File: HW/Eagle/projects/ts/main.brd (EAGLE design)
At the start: 80 x 45 mm, 46 parts, among them IC1 4050D, Q1 20 MHz, T1 IRFZ24N, T2 IRFZ24N, U1 ATMEGA328P-PU, U2 LM2576T, U3 HT7533, U4 LM75

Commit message: [HW] Minor change
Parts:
- removed R5: 0R, rcl:R0805
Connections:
- removed net N$1: C9.+, R5.2, U3.3
- net +3V3: now also C9.+, U3.3; no longer R5.1
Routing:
- net +3V3: track 29.6 -> 38.8 mm
- net N$1: track 7.34 -> 0.00 mm
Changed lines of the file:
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@@
 <attribute name="OC_NEWARK" value="unknown" x="34.5" y="39.5" size="1.778" layer="27" display="off"/>
-</element>
-<element name="R5" library="rcl" package="R0805" value="0R" x="11" y="40.5" smashed="yes" rot="R180">
-<attribute name="NAME" x="9.365" y="41.77" size="1.27" layer="25"/>
-<attribute name="VALUE" x="11.635" y="43.04" size="1.27" layer="27" rot="R180"/>
 </element>
 <element name="C11" library="rcl" package="C0805" value="100nF" x="29" y="30" smashed="yes" rot="R90">
@@
 <contactref element="RESET" pad="3"/>
 <via x="9.5" y="38.75" extent="1-16" drill="0.5"/>
-<via x="6" y="41" extent="1-16" drill="0.5"/>
+<via x="5" y="41" extent="1-16" drill="0.5"/>
 <via x="5" y="31" extent="1-16" drill="0.5"/>
-<via x="12.5" y="38.75" extent="1-16" drill="0.5"/>
+<via x="9.25" y="44" extent="1-16" drill="0.5"/>
 <contactref element="IC1" pad="7"/>
 <contactref element="UART" pad="1"/>
@@
 <via x="45" y="6" extent="1-16" drill="0.5"/>
 <via x="40.5" y="1.5" extent="1-16" drill="0.5"/>
-<via x="7.5" y="35.5" extent="1-16" drill="0.5"/>
+<via x="7.5" y="36" extent="1-16" drill="0.5"/>
 <via x="57.25" y="32.25" extent="1-16" drill="0.5"/>
 <via x="41.25" y="9.75" extent="1-16" drill="0.5"/>
@@
 <wire x1="28" y1="26" x2="24" y2="22" width="1.3" layer="16"/>
 <wire x1="24" y1="22" x2="19.5" y2="22" width="1.3" layer="16"/>
-<wire x1="11.46" y1="26.5" x2="11.46" y2="31.04" width="0.4" layer="16"/>
-<wire x1="11.46" y1="31.04" x2="11" y2="31.5" width="0.4" layer="16"/>
-<wire x1="11" y1="31.5" x2="11" y2="34.595" width="0.4" layer="16"/>
 <wire x1="17.55" y1="43" x2="12.5" y2="43" width="0.25" layer="1"/>
 <wire x1="12.5" y1="43" x2="12" y2="42.5" width="0.25" layer="1"/>
@@
 <wire x1="62.375" y1="18.125" x2="63.425" y2="18.125" width="1" layer="16"/>
 <wire x1="63.425" y1="18.125" x2="63.5" y2="18.2" width="1" layer="16"/>
+<wire x1="11.46" y1="26.5" x2="11.46" y2="31.04" width="0.5" layer="16"/>
+<wire x1="11.46" y1="31.04" x2="11" y2="31.5" width="0.5" layer="16"/>
+<wire x1="11" y1="31.5" x2="11" y2="34.595" width="0.5" layer="16"/>
 </signal>
 <signal name="AREF">
@@
 <contactref element="IC1" pad="1"/>
 <contactref element="LCD" pad="1"/>
-<contactref element="R5" pad="1"/>
 <contactref element="C11" pad="2"/>
-<wire x1="11.95" y1="40.5" x2="12" y2="40.5" width="0.4" layer="1"/>
 <wire x1="29" y1="30.95" x2="29" y2="35" width="0.25" layer="1"/>
 <wire x1="29" y1="30.95" x2="30.05" y2="30.95" width="0.25" layer="1"/>
@@
 <wire x1="30.5" y1="30.5" x2="30.5" y2="29.4816" width="0.25" layer="1"/>
 <wire x1="30.5" y1="29.4816" x2="31.055" y2="28.9266" width="0.25" layer="1"/>
-<via x="15.5" y="37" extent="1-16" drill="0.35"/>
-<wire x1="11.95" y1="40.5" x2="12.85" y2="39.6" width="0.4" layer="1"/>
-<wire x1="12.85" y1="39.6" x2="12.8520875" y2="39.6" width="0.4" layer="1"/>
-<wire x1="15.4520875" y1="37" x2="15.5" y2="37" width="0.4" layer="1"/>
-<wire x1="12.8520875" y1="39.6" x2="15.4520875" y2="37" width="0.4" layer="1"/>
-<wire x1="15.5" y1="37" x2="23.11" y2="37" width="0.4" layer="16"/>
-<wire x1="23.11" y1="37" x2="25.61" y2="39.5" width="0.4" layer="16"/>
 <wire x1="29" y1="35" x2="25.61" y2="38.39" width="0.25" layer="1"/>
 <wire x1="25.61" y1="38.39" x2="25.61" y2="39.5" width="0.25" layer="1"/>
-</signal>
-<signal name="N$1">
 <contactref element="U3" pad="3"/>
 <contactref element="C9" pad="+"/>
-<contactref element="R5" pad="2"/>
-<wire x1="9.73" y1="36.5" x2="9.55" y2="36.5" width="0.4" layer="1"/>
-<wire x1="9.55" y1="36.5" x2="7.05" y2="39" width="0.4" layer="1"/>
-<wire x1="7.05" y1="39" x2="8.55" y2="40.5" width="0.4" layer="1"/>
-<wire x1="8.55" y1="40.5" x2="10.05" y2="40.5" width="0.4" layer="1"/>
+<wire x1="9.73" y1="36.5" x2="7.23" y2="39" width="0.5" layer="1"/>
+<wire x1="7.23" y1="39" x2="7.05" y2="39" width="0.5" layer="1"/>
+<wire x1="7.05" y1="39" x2="8.55" y2="40.5" width="0.5" layer="1"/>
+<via x="15.5" y="37" extent="1-16" drill="0.35"/>
+<wire x1="13.4" y1="39.12279375" x2="13.4" y2="39.1" width="0.5" layer="1"/>
+<wire x1="13.4" y1="39.1" x2="15.5" y2="37" width="0.5" layer="1"/>
+<wire x1="8.55" y1="40.5" x2="12.02279375" y2="40.5" width="0.5" layer="1"/>
+<wire x1="12.02279375" y1="40.5" x2="13.4" y2="39.12279375" width="0.5" layer="1"/>
+<wire x1="15.5" y1="37" x2="23.11" y2="37" width="0.5" layer="16"/>
+<wire x1="23.11" y1="37" x2="25.61" y2="39.5" width="0.5" layer="16"/>
 </signal>
 <signal name="LCD_SCE">
@@
 <contactref element="R11" pad="2"/>
 <wire x1="39.91" y1="18.46" x2="40" y2="18.55" width="0.25" layer="1"/>
-<wire x1="38.75" y1="9.75" x2="39.75" y2="8.75" width="0.25" layer="1"/>
+<wire x1="39.75" y1="8.75" x2="38.75" y2="9.75" width="0.25" layer="1"/>
 <wire x1="38.75" y1="9.75" x2="38.75" y2="17.25" width="0.25" layer="1"/>
 <wire x1="38.75" y1="17.25" x2="37.54" y2="18.46" width="0.25" layer="1"/>

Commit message: [HW] Organized schematics
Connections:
- net AREF renamed N$1
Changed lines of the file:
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@@
 <?xml version="1.0" encoding="utf-8"?>
 <!DOCTYPE eagle SYSTEM "eagle.dtd">
-<eagle version="8.5.0">
+<eagle version="8.7.1">
 <drawing>
 <settings>
@@
 <via x="64" y="40.5" extent="1-16" drill="0.5"/>
 <via x="20" y="13" extent="1-16" drill="0.5"/>
-<contactref element="C1" pad="2"/>
 <via x="48.5" y="17" extent="1-16" drill="0.5"/>
 <contactref element="C11" pad="1"/>
@@
 <via x="22.5" y="44" extent="1-16" drill="0.5"/>
 <via x="40.5" y="25.5" extent="1-16" drill="0.5"/>
+<contactref element="C1" pad="2"/>
 </signal>
 <signal name="VCC">
@@
 <wire x1="11" y1="31.5" x2="11" y2="34.595" width="0.5" layer="16"/>
 </signal>
-<signal name="AREF">
-<contactref element="U1" pad="21"/>
-<contactref element="C1" pad="1"/>
-<wire x1="66.55" y1="20.5" x2="63.74" y2="20.5" width="0.7" layer="1"/>
-<wire x1="63.74" y1="20.5" x2="63.5" y2="20.74" width="0.7" layer="1"/>
-</signal>
 <signal name="N$3">
 <contactref element="Q1" pad="1"/>
@@
 <wire x1="48.25" y1="9.25" x2="50.05" y2="9.25" width="0.25" layer="1"/>
 </signal>
+<signal name="N$1">
+<contactref element="U1" pad="21"/>
+<contactref element="C1" pad="1"/>
+<wire x1="66.55" y1="20.5" x2="63.74" y2="20.5" width="1" layer="1"/>
+<wire x1="63.74" y1="20.5" x2="63.5" y2="20.74" width="1" layer="1"/>
+</signal>
 </signals>

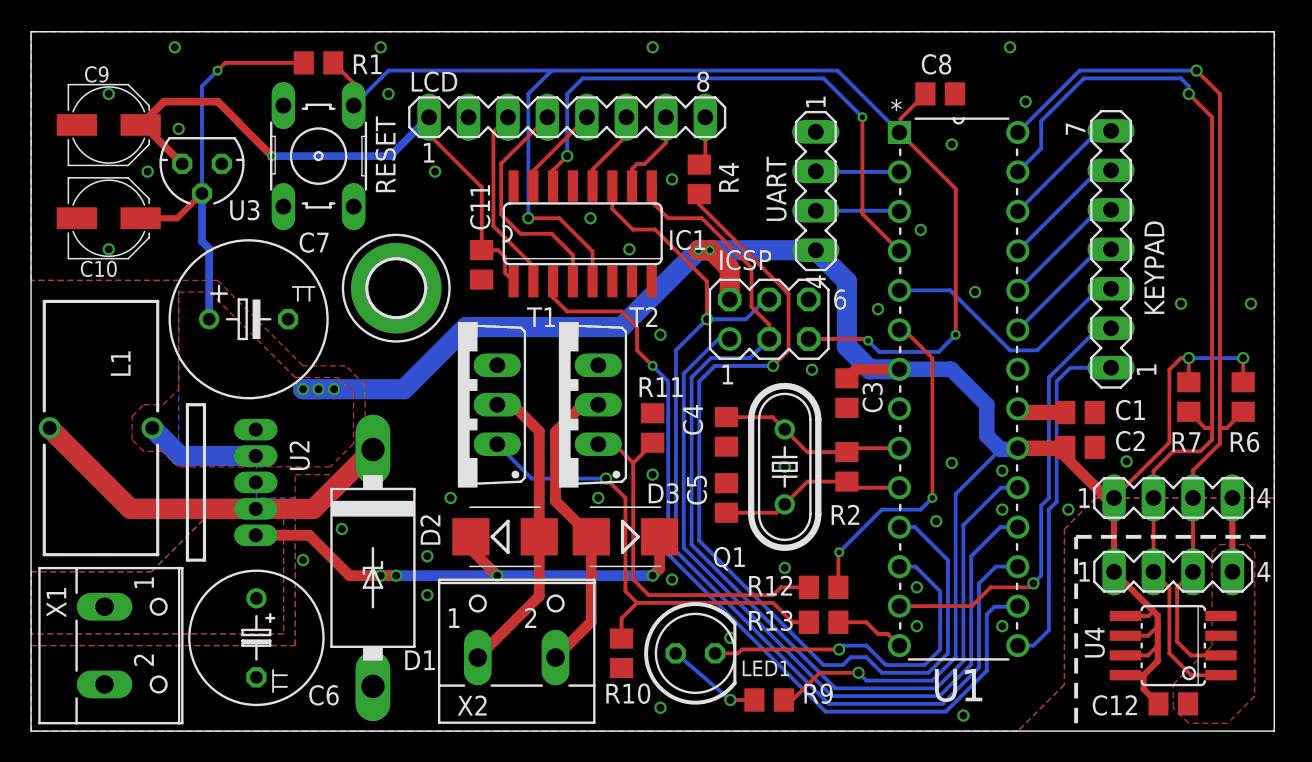
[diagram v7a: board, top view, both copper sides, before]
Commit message: [HW] Resolved some design DRC and ERC warnings
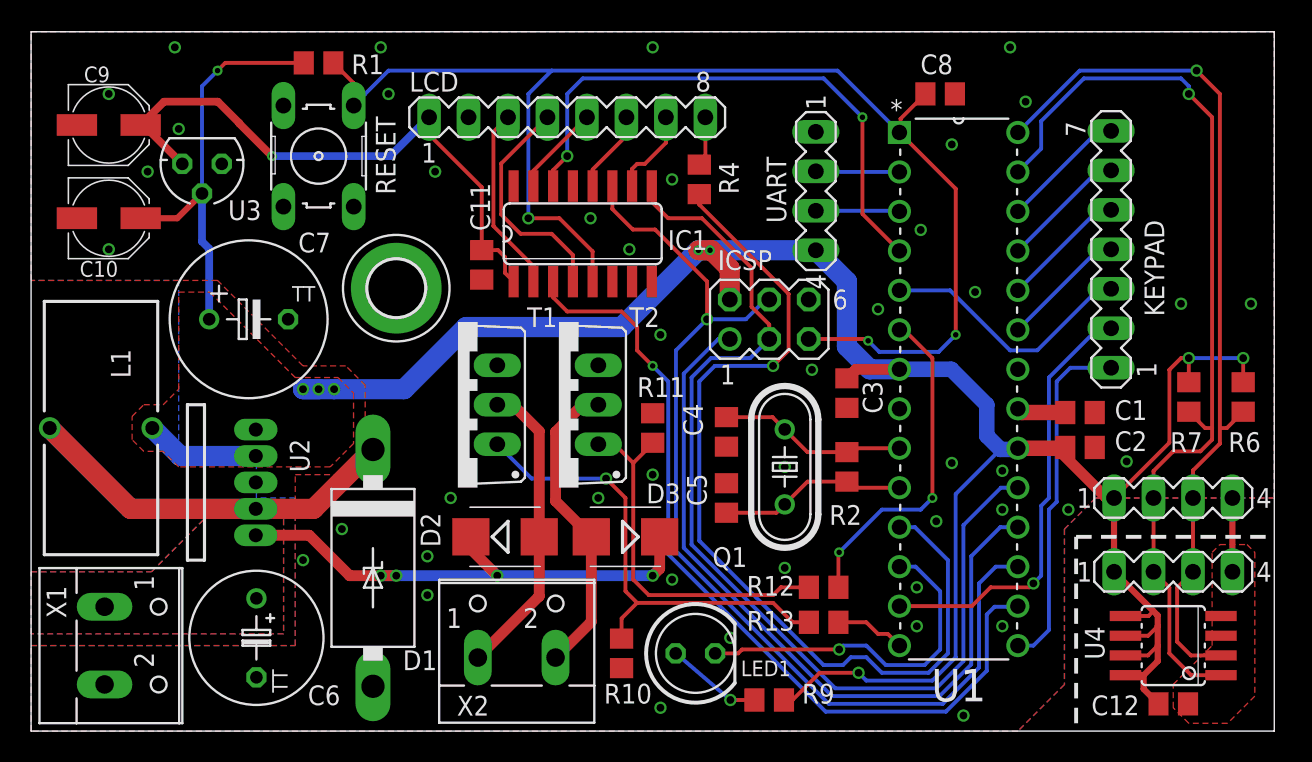
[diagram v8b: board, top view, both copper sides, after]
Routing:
- net MOSI: track 65.8 -> 65.1 mm
- net VCC: track 178.8 -> 178.3 mm
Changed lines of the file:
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@@
 <?xml version="1.0" encoding="utf-8"?>
 <!DOCTYPE eagle SYSTEM "eagle.dtd">
-<eagle version="8.7.1">
+<eagle version="9.2.2">
 <drawing>
 <settings>
@@
 <param name="checkStop" value="0"/>
 <param name="checkValues" value="0"/>
+<param name="checkNames" value="1"/>
+<param name="checkWireStubs" value="1"/>
+<param name="checkPolygonWidth" value="0"/>
 <param name="useDiameter" value="13"/>
 <param name="maxErrors" value="50"/>
@@
 <attribute name="VALUE" x="10.698" y="23.452" size="1.27" layer="27" ratio="10"/>
 </element>
-<element name="L1" library="rcl" package="TJ3-U1" value="100uH" x="4.5" y="19.5" rot="R180"/>
-<element name="X1" library="con-wago-500" package="W237-102" value="" x="6" y="5.5" rot="R270">
+<element name="L1" library="rcl" package="TJ3-U1" value="100uH" x="4.5" y="19.5" smashed="yes" rot="R180">
+<attribute name="NAME" x="5.135" y="24.58" size="1.27" layer="25" rot="R270"/>
+<attribute name="VALUE" x="2.595" y="24.58" size="1.27" layer="27" rot="R270"/>
+</element>
+<element name="X1" library="con-wago-500" package="W237-102" value="" x="6" y="5.5" smashed="yes" rot="R270">
 <attribute name="MF" value="" x="6" y="5.5" size="1.778" layer="27" rot="R270" display="off"/>
 <attribute name="MPN" value="237-102" x="6" y="5.5" size="1.778" layer="27" rot="R270" display="off"/>
+<attribute name="NAME" x="0.9962" y="9.3462" size="1.27" layer="25" ratio="10" rot="R270"/>
 <attribute name="OC_FARNELL" value="unknown" x="6" y="5.5" size="1.778" layer="27" rot="R270" display="off"/>
 <attribute name="OC_NEWARK" value="70K9898" x="6" y="5.5" size="1.778" layer="27" rot="R270" display="off"/>
-</element>
-<element name="X2" library="con-wago-500" package="W237-102" value="" x="31.25" y="6">
+<attribute name="VALUE" x="-1.62" y="10.54" size="1.27" layer="27" ratio="10" rot="R270"/>
+</element>
+<element name="X2" library="con-wago-500" package="W237-102" value="" x="31.25" y="6" smashed="yes">
 <attribute name="MF" value="" x="31.25" y="6" size="1.778" layer="27" display="off"/>
 <attribute name="MPN" value="237-102" x="31.25" y="6" size="1.778" layer="27" display="off"/>
+<attribute name="NAME" x="27.4038" y="0.9962" size="1.27" layer="25" ratio="10"/>
 <attribute name="OC_FARNELL" value="unknown" x="31.25" y="6" size="1.778" layer="27" display="off"/>
 <attribute name="OC_NEWARK" value="70K9898" x="31.25" y="6" size="1.778" layer="27" display="off"/>
+<attribute name="VALUE" x="26.21" y="-1.62" size="1.27" layer="27" ratio="10"/>
 </element>
 <element name="C8" library="rcl" package="C0805" value="100nF" x="58.5" y="41" smashed="yes" rot="R180">
@@
 <attribute name="VALUE" x="31.436" y="31.365" size="1.27" layer="27" ratio="10"/>
 </element>
-<element name="LCD" library="con-lstb" package="MA08-1" value="" x="34.5" y="39.5">
+<element name="LCD" library="con-lstb" package="MA08-1" value="" x="34.5" y="39.5" smashed="yes">
 <attribute name="MF" value="" x="34.5" y="39.5" size="1.778" layer="27" display="off"/>
 <attribute name="MPN" value="" x="34.5" y="39.5" size="1.778" layer="27" display="off"/>
+<attribute name="NAME" x="24.34" y="41.151" size="1.27" layer="25" ratio="10"/>
 <attribute name="OC_FARNELL" value="unknown" x="34.5" y="39.5" size="1.778" layer="27" display="off"/>
 <attribute name="OC_NEWARK" value="unknown" x="34.5" y="39.5" size="1.778" layer="27" display="off"/>
+<attribute name="VALUE" x="33.23" y="36.579" size="1.27" layer="27" ratio="10"/>
 </element>
 <element name="C11" library="rcl" package="C0805" value="100nF" x="29" y="30" smashed="yes" rot="R90">
@@
 <attribute name="VALUE" x="45.9504" y="3.1966" size="1.27" layer="27" ratio="10"/>
 </element>
-<element name="H1" library="holes" package="3,6-PAD" value="MOUNT-PAD-ROUND3.6" x="23.5" y="28.5"/>
+<element name="H1" library="holes" package="3,6-PAD" value="MOUNT-PAD-ROUND3.6" x="23.5" y="28.5" smashed="yes"/>
 <element name="TEMP_A" library="con-lstb" library_urn="urn:adsk.eagle:library:162" package="MA04-1" package3d_urn="urn:adsk.eagle:package:8337/1" value="" x="73.5" y="10.25" smashed="yes">
 <attribute name="MF" value="" x="73.5" y="10.25" size="1.778" layer="27" display="off"/>
@@
 <wire x1="52.5" y1="24.75" x2="53.97" y2="23.28" width="1.3" layer="16"/>
 <wire x1="53.97" y1="23.28" x2="55.88" y2="23.28" width="1.3" layer="16"/>
-<wire x1="48.45" y1="2" x2="48.45" y2="1.5" width="0.25" layer="1"/>
 <via x="53.25" y="3.75" extent="1-16" drill="0.5" diameter="0.8"/>
 <wire x1="53.25" y1="3.75" x2="50.75" y2="3.75" width="0.25" layer="1"/>
@@
 <wire x1="40" y1="10" x2="30" y2="10" width="0.7" layer="16"/>
 <via x="30" y="10" extent="1-16" drill="0.5"/>
-<wire x1="28.2" y1="12.6" x2="28.3" y2="12.5" width="0.7" layer="1"/>
 <wire x1="28.3" y1="12.5" x2="28.3" y2="11.7" width="0.7" layer="1"/>
 <wire x1="28.3" y1="11.7" x2="30" y2="10" width="0.7" layer="1"/>
@@
 <contactref element="U1" pad="17"/>
 <contactref element="IC1" pad="11"/>
-<wire x1="37.405" y1="35.0734" x2="37.405" y2="34.345" width="0.25" layer="1"/>
 <wire x1="37.405" y1="35.0734" x2="37.405" y2="33.595" width="0.25" layer="1"/>
 <via x="43.5" y="26.5" extent="1-16" drill="0.5"/>
@@
 <wire x1="73.75" y1="9.23" x2="74.77" y2="10.25" width="0.25" layer="1"/>
 <wire x1="76.5" y1="19.5" x2="76.5" y2="18.5" width="0.25" layer="1"/>
-<wire x1="76.5" y1="40" x2="76.5" y2="19.5" width="0.25" layer="1"/>
-<wire x1="76.5" y1="40" x2="76.5" y2="40.25" width="0.25" layer="1"/>
+<wire x1="76.5" y1="41" x2="76.5" y2="19.5" width="0.25" layer="1"/>
 <wire x1="74.77" y1="15" x2="74.77" y2="16.77" width="0.25" layer="1"/>
 <wire x1="74.77" y1="16.77" x2="76.5" y2="18.5" width="0.25" layer="1"/>
@@
 <wire x1="63.5" y1="38.52" x2="67.48" y2="42.5" width="0.25" layer="16"/>
 <via x="75" y="42.5" extent="1-16" drill="0.5" diameter="0.8"/>
-<wire x1="75" y1="42.5" x2="76.5" y2="41" width="0.25" layer="1"/>
-<wire x1="76.5" y1="41" x2="76.5" y2="40" width="0.25" layer="1"/>
+<wire x1="76.5" y1="41" x2="75" y2="42.5" width="0.25" layer="1"/>
 <wire x1="67.48" y1="42.5" x2="75" y2="42.5" width="0.25" layer="16"/>
 </signal>
@@
 <contactref element="T2" pad="G"/>
 <contactref element="R11" pad="2"/>
-<wire x1="39.91" y1="18.46" x2="40" y2="18.55" width="0.25" layer="1"/>
 <wire x1="39.75" y1="8.75" x2="38.75" y2="9.75" width="0.25" layer="1"/>
 <wire x1="38.75" y1="9.75" x2="38.75" y2="17.25" width="0.25" layer="1"/>
@@
 </signal>
 </signals>
+<mfgpreviewcolors>
+<mfgpreviewcolor name="soldermaskcolor" color="0xC8008000"/>
+<mfgpreviewcolor name="silkscreencolor" color="0xFFFEFEFE"/>
+<mfgpreviewcolor name="backgroundcolor" color="0xFF282828"/>
+<mfgpreviewcolor name="coppercolor" color="0xFFFFBF00"/>
+<mfgpreviewcolor name="substratecolor" color="0xFF786E46"/>
+</mfgpreviewcolors>
 </board>
 </drawing>
